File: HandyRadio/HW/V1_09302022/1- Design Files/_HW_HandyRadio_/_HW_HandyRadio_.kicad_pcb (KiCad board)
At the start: 4 copper layers, 74.9 x 74.9 mm, 172 parts, among them J1 MHDR_4POS_1ROW, J2 RECEP_6POS_1ROW, J3 AUDIO_Jack, J4 USB_uAB_RECEP, J5 XH_CONN_2POS_R/A, J6 MHDR_2POS_VERT, K1 DPDT_RELAY, Q1 IRF7401TRPBF, Q2 MMUN2215LT1G, SW1 SPST_NO_RA, SW2 SPST_NO_RA, SW3 SPST_NO_RA, U1 STM32F030F4P6, U2 IR_REC_38KHz, U3 LM4808, U4 MCP73831, U5 AP7361EA, U6 R1211N002B, U7 MIC5365-3.3, U8 EGUARD0502A, U9 SI4735-D60-GU

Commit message: doing placement
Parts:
- C19, C20, C21, C31, C32, C33, C35, C37, C40, D2, EC2, J4, R17, R18, R26, R28, R29, R30, R31, R32: moved to B.Cu
- moved R21 148.1 mm to (201.9, 171.4), turned to 180 degrees
- moved EC5 146.9 mm to (201.9, 168.3), turned to 180 degrees
- moved C20 144.0 mm to (208.9, 163.2), turned to -90 degrees
- moved C19 138.8 mm to (205.1, 163.2), turned to -90 degrees
- moved EC6 137.3 mm to (201.9, 165.1), turned to 180 degrees
- moved R22 136.3 mm to (201.9, 161.9), turned to 180 degrees
- moved R16 135.1 mm to (209.6, 172.7), turned to 180 degrees
- moved EC2 134.7 mm to (208.9, 167.6), turned to -90 degrees
- moved C21 133.8 mm to (205.1, 167.6), turned to 90 degrees
- moved C41 133.2 mm to (160.6, 124.7)
- moved R27 133.2 mm to (154.9, 145.0)
- moved TP16 133.2 mm to (179.1, 125.2)
- moved C39 133.2 mm to (175.1, 121.9)
- moved EC11 133.2 mm to (148.8, 132.1)
- moved EC9 133.2 mm to (140.5, 145.7)
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
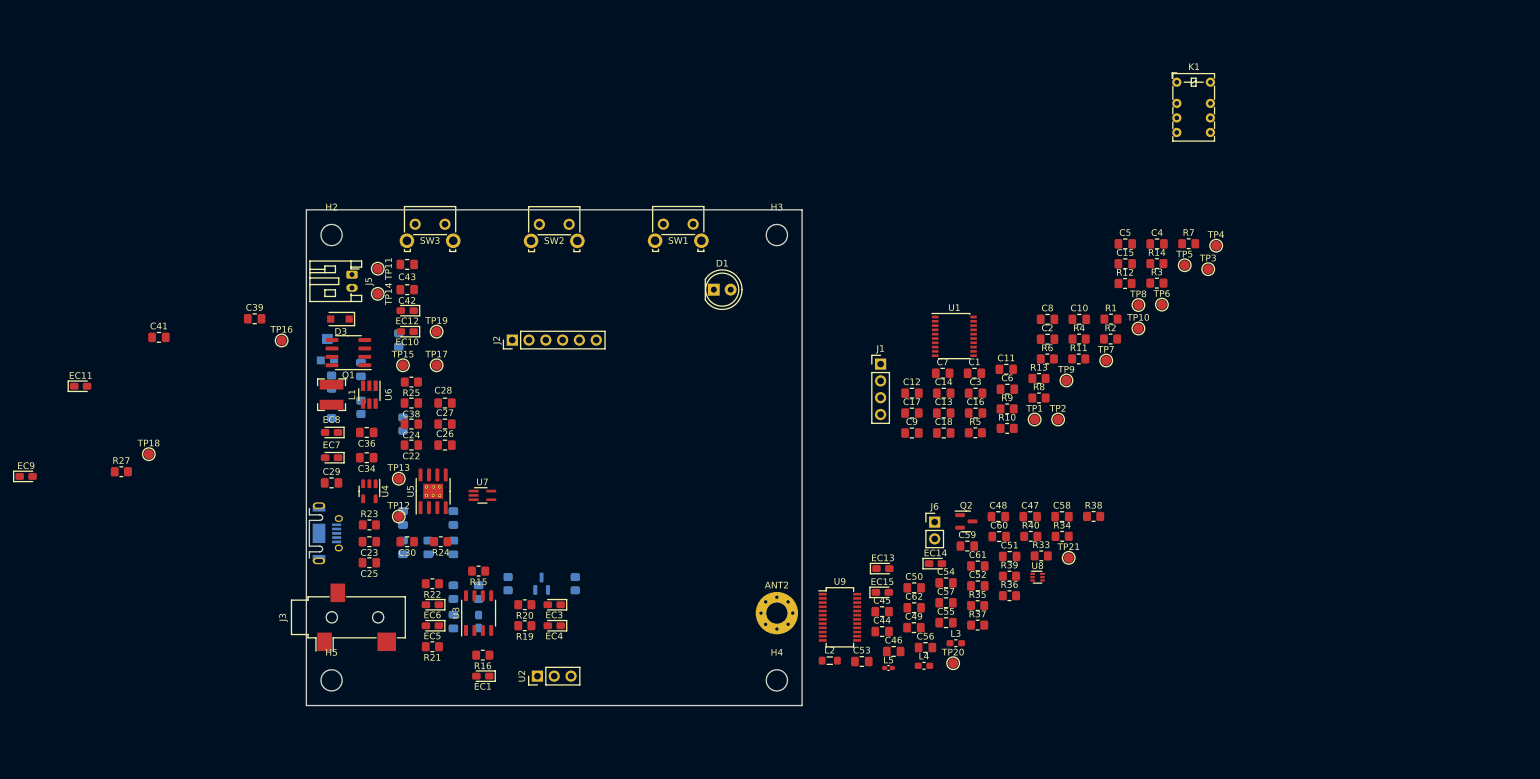
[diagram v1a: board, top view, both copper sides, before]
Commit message: Placement is almost done
Just it needs to checking the footprints, add some 3d and doing routing!
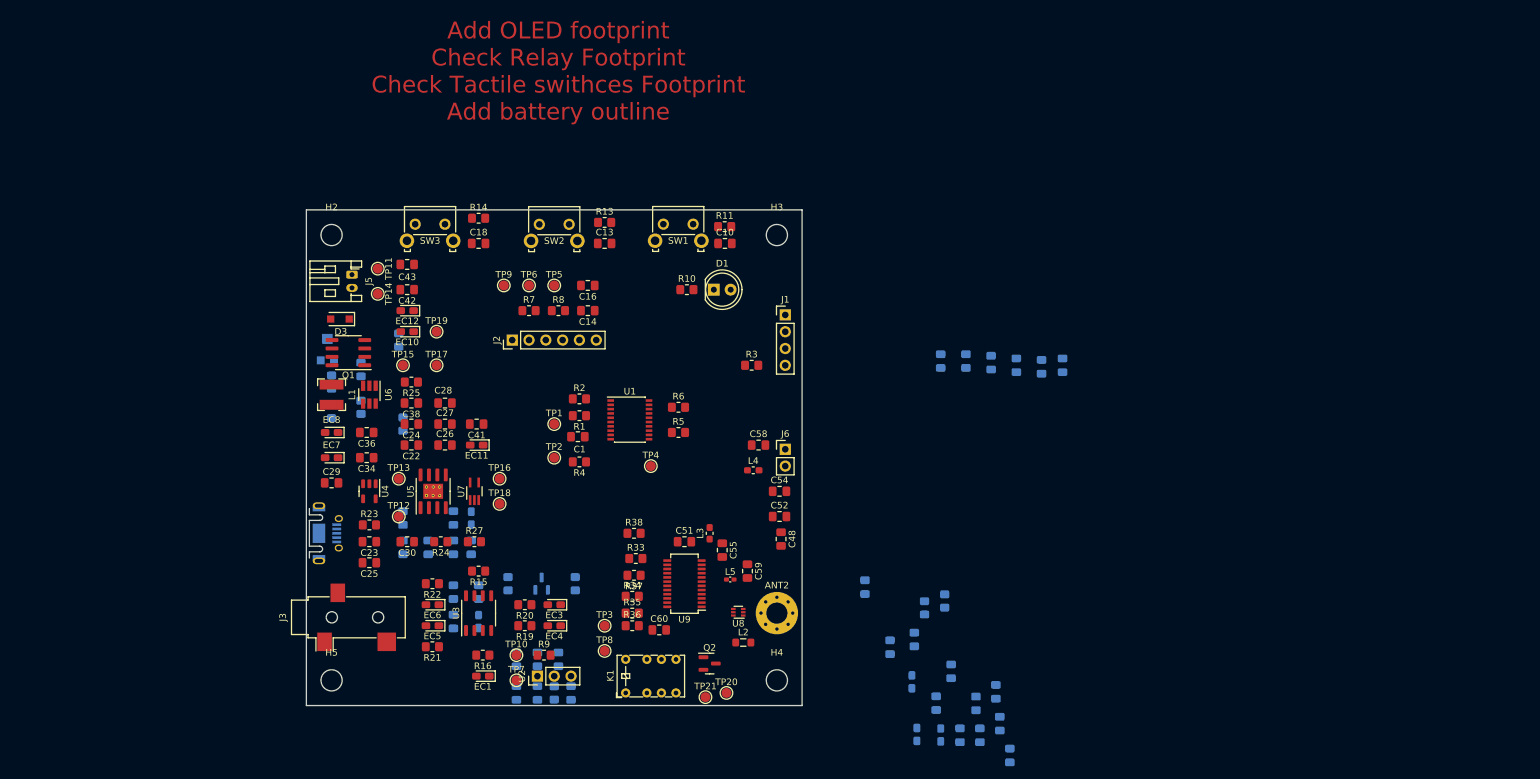
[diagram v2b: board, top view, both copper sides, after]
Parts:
- C11, C12, C15, C17, C2, C3, C39, C4, C44, C45, C46, C47, C49, C5, C50, C53, C56, C57, C6, C61, C62, C7, C8, C9, EC13, EC14, EC15, EC9, R12, R39, R40: moved to B.Cu
- moved K1 124.3 mm to (231.2, 178.4), turned to 90 degrees
- moved C15 109.7 mm to (214.6, 173.4), turned to -90 degrees
- moved TP10 106.2 mm to (214.6, 172.7)
- moved R12 106.2 mm to (220.3, 178.4), turned to -90 degrees
- moved TP3 106.0 mm to (228.0, 168.3)
- moved R14 102.8 mm to (208.9, 106.7)
- moved TP7 101.4 mm to (214.6, 176.5)
- moved R7 100.2 mm to (216.5, 120.7)
- moved C8 98.2 mm to (214.6, 178.4), turned to 90 degrees
- moved TP8 96.1 mm to (228.0, 172.1)
- moved TP6 95.7 mm to (216.5, 116.8)
- moved TP5 95.4 mm to (220.3, 116.8)
- moved TP4 91.7 mm to (234.9, 144.1)
- moved TP9 86.2 mm to (212.7, 116.8)
- moved C11 83.3 mm to (217.8, 173.4), turned to -90 degrees
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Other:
- board text added: "Add OLED footprint Check Relay Footprint Check Tactile swithces Footprint Add battery outline"

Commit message: Working on lib and pcb layout
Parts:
- added DIS1: OLED, _HW_HandyRadio_Footprint:OLED 1.3INCH, F.Cu at (202.7, 126.1)
- J3: footprint Connector_Audio:Jack_3.5mm_CUI_SJ-3523-SMT_Horizontal -> _HW_HandyRadio_Footprint:Jack_3.5mm_CUI_SJ-3524-SMT_Horizontal
- J4: footprint Connector_USB:USB_Micro-AB_Molex_47590-0001 -> _HW_HandyRadio_Footprint:USB_Micro-AB_Molex_47590-0001
- R30: footprint Potentiometer_SMD:Potentiometer_Bourns_TC33X_Vertical -> _HW_HandyRadio_Footprint:Potentiometer_Bourns_TC33X_Vertical
- SW1, SW2, SW3: footprint Button_Switch_THT:SW_Tactile_SKHH_Angled -> _HW_HandyRadio_Footprint:SW_Tact_SKHH_Angled
- U3: footprint Package_SO:SOP-8_3.9x4.9mm_P1.27mm -> _HW_HandyRadio_Footprint:SOP-8_3.9x4.9mm_P1.27mm
- U5: footprint Package_SO:SOIC-8-1EP_3.9x4.9mm_P1.27mm_EP2.29x3mm_ThermalVias -> _HW_HandyRadio_Footprint:Infineon_PG-DSO-8-27_3.9x4.9mm_EP2.65x3mm_ThermalVias
- moved U5 4.13 mm to (199.6, 151.2)
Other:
- board text added: "Add OLED footprint Check Relay Footprint Add battery outline"
- board text removed: "Add OLED footprint Check Relay Footprint Check Tactile swithces Footprint Add battery outline"

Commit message: Some work on PCB, it's paused and will be continued later on
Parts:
- moved TP21 15.4 mm to (227.8, 178.6)
- moved TP20 14.6 mm to (231.8, 178.3)
- moved C51 14.5 mm to (254.3, 158.5)
- moved R33 14.3 mm to (240.3, 146.1)
- moved Q2 14.2 mm to (229.6, 174.2)
- moved R38 14.0 mm to (240.3, 142.7), turned to 180 degrees
- moved R37 13.8 mm to (240.3, 149.4)
- moved R34 13.6 mm to (240.3, 152.9)
- moved R35 13.0 mm to (240.3, 156.2)
- moved U9 12.6 mm to (247.9, 152.1)
- moved TP8 12.1 mm to (236.0, 163.1)
- moved R36 11.8 mm to (240.3, 159.8)
- moved L5 11.3 mm to (254.3, 152.7), turned to 180 degrees
- moved L3 10.6 mm to (254.3, 156.5), turned to 180 degrees
- moved C59 10.3 mm to (254.3, 150.9), turned to 180 degrees
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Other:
- board text added: "Check Relay Footprint"
- board text removed: "Add OLED footprint Check Relay Footprint Add battery outline"

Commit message: serious modification has been done
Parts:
- removed D3: DSS13U, Diode_SMD:D_SOD-123F
- removed EC10, EC12, EC15, EC9: 2u2F/10V, Capacitor_Tantalum_SMD:CP_EIA-2012-12_Kemet-R_Pad1.30x1.05mm_HandSolder
- removed EC11, EC13, EC14, EC7, EC8: 4u7F/6.3V, Capacitor_Tantalum_SMD:CP_EIA-2012-12_Kemet-R_Pad1.30x1.05mm_HandSolder
- removed R40: 330R, Resistor_SMD:R_0805_2012Metric_Pad1.20x1.40mm_HandSolder
- added C63: 6pF, Capacitor_SMD:C_0805_2012Metric_Pad1.18x1.45mm_HandSolder, F.Cu at (255.0, 159.5)
- added C64: 10nF, Capacitor_SMD:C_0805_2012Metric_Pad1.18x1.45mm_HandSolder, B.Cu at (244.3, 156.0)
- added C65: 22nF, Capacitor_SMD:C_0805_2012Metric_Pad1.18x1.45mm_HandSolder, B.Cu at (240.8, 156.0)
- added C66: 3p3F, Capacitor_SMD:C_0805_2012Metric_Pad1.18x1.45mm_HandSolder, F.Cu at (255.0, 149.9)
- added C67: 6pF, Capacitor_SMD:C_0805_2012Metric_Pad1.18x1.45mm_HandSolder, F.Cu at (255.0, 153.4)
- added C68: 22nF, Capacitor_SMD:C_0805_2012Metric_Pad1.18x1.45mm_HandSolder, F.Cu at (241.3, 157.5)
- added C69: 33pF, Capacitor_SMD:C_0805_2012Metric_Pad1.18x1.45mm_HandSolder, B.Cu at (252.0, 155.4)
- added C70: 33pF, Capacitor_SMD:C_0805_2012Metric_Pad1.18x1.45mm_HandSolder, B.Cu at (255.5, 155.4)
- C10, C17, C53: value 100nF -> 10uF
- C11, C49: value 10uF -> 4u7F; moved to F.Cu
- C12, C2, C20, C3, C32, C39, C4, C9, J4: moved to F.Cu
- C13, C16, C25, C26, Q2, R14, R24, R27, R9: moved to B.Cu
- C14: value 4u7F -> 100nF
- C15, C50: value 10uF -> 100nF; moved to F.Cu
- C18, C28, C41: value 100nF -> 1uF; moved to B.Cu
- C19, C22, C30: value 1uF -> 100nF
- C21: value 10nF -> 100nF; moved to F.Cu
- C23: value 4u7F -> 10nF
- C27: value 1uF -> 4u7F; moved to B.Cu
- C29, C34, C42: value 4u7F -> 1uF; moved to B.Cu
- C31: value 1uF -> 4u7F; moved to F.Cu
- C37: value 100nF -> 1uF
- C38: value 220nF -> 4u7F
- C40: value 680pF -> 220nF
- C43: value 4u7F -> 100nF; moved to B.Cu
- C44: value 10uF -> 680pF; moved to F.Cu
- C45: value 10uF -> 1uF
- C46: value 100nF -> 1uF; moved to F.Cu
- C47: value 22nF -> 1uF
- C48: value 33pF -> 1uF
- C5: value 4u7F -> 100nF; moved to F.Cu
- C51: value 18pF -> 4u7F
- C52: value 470nF -> 10uF; moved to B.Cu
- C54: value 3p3F -> 100nF; moved to B.Cu
- C55: value 6pF -> 22nF; moved to B.Cu
- C56: value 10nF -> 33pF; moved to F.Cu
- C57: value 22nF -> 10uF
- C58: value 3p3F -> 10uF; moved to B.Cu
- C59: value 6pF -> 18pF
- C6: value 100nF -> 10uF; moved to F.Cu
- C60: value 22nF -> 470nF
- C61: value 33pF -> 100nF
- C62: value 33pF -> 3p3F; moved to F.Cu
- C7: value 10nF -> 10uF; moved to F.Cu
- C8: value 10uF -> 100nF
- D2: value BAT54ATA -> DSS13U; footprint Package_TO_SOT_SMD:SOT-23 -> Diode_SMD:D_SOD-123F; moved to F.Cu
- EC1: value 1uF/16V -> 4u7F/6.3V
- EC2: value 4u7F/6.3V -> 2u2F/10V; moved to F.Cu
- EC4: value 2u2F/10V -> 4u7F/6.3V; moved to B.Cu
- EC5: value 100uF/6.3V -> 4u7F/6.3V; moved to B.Cu
- EC6: value 100uF/6.3V -> 2u2F/10V; moved to B.Cu
- J3: value AUDIO_Jack -> XH_CONN_2POS_R/A; footprint _HW_HandyRadio_Footprint:Jack_3.5mm_CUI_SJ-3524-SMT_Horizontal -> Connector_JST:JST_PH_S2B-PH-K_1x02_P2.00mm_Horizontal
- K1: footprint Relay_THT:Relay_DPDT_AXICOM_IMSeries_Pitch5.08mm -> Relay_THT:Relay_DPDT_Finder_30.22
- R10: value 1KR -> 10KR; moved to B.Cu
- R11: value 10KR -> 1KR
- R12, R5: value 47R -> 10KR
- R13, R4: value 10KR -> 47R
- R15, R16: value 100KR -> 10KR; moved to B.Cu
- R17, R18: value 1KR -> 3K9R; moved to F.Cu
- R19, R22: value 3K9R -> 10KR
- R20: value 3K9R -> 2KR
- R21: value 3K9R -> 100KR; moved to B.Cu
- R23: value 2KR -> 10KR
- R25: value 100KR -> 30KR
- R26: value 30KR -> 10KR; moved to F.Cu
- R28, R33: value 10KR -> 2KR
- R29: value 2KR -> POT_5KR; footprint Resistor_SMD:R_0805_2012Metric_Pad1.20x1.40mm_HandSolder -> _HW_HandyRadio_Footprint:Potentiometer_Bourns_TC33X_Vertical
- R3: value 1KR -> 10KR
- R30: value POT_5KR -> 82KR; footprint _HW_HandyRadio_Footprint:Potentiometer_Bourns_TC33X_Vertical -> Resistor_SMD:R_0805_2012Metric_Pad1.20x1.40mm_HandSolder; moved to F.Cu
- R31: value 82KR -> 16KR5; moved to F.Cu
- R32: value 16KR5 -> 10KR; moved to F.Cu
- R36: value 2KR -> 100KR
- R37: value 100KR -> 2KR
- R38: value 2KR -> 330R; moved to B.Cu
- U1: value STM32F030F4P6 -> PIC16F15223; footprint Package_SO:SSOP-20_4.4x6.5mm_P0.65mm -> Package_SO:SO-14_3.9x8.65mm_P1.27mm
- U3: value LM4808 -> PAM8302AASCR; footprint _HW_HandyRadio_Footprint:SOP-8_3.9x4.9mm_P1.27mm -> Package_SO:MSOP-8_3x3mm_P0.65mm
- moved C46 104.1 mm to (208.3, 115.8), turned to 180 degrees
- moved C45 97.7 mm to (205.2, 124.0), turned to 90 degrees
- moved C49 97.1 mm to (195.1, 141.2), turned to 0 degrees
- moved C44 92.6 mm to (197.6, 153.4), turned to 0 degrees
- moved C50 90.1 mm to (208.3, 122.9), turned to 180 degrees
- moved C5 87.4 mm to (208.3, 146.3), turned to 180 degrees
- moved C4 82.2 mm to (215.4, 137.2), turned to 0 degrees
- moved C6 74.8 mm to (221.5, 165.6), turned to 0 degrees
- moved C2 70.2 mm to (220.5, 137.2), turned to 180 degrees
- moved C47 70.1 mm to (208.8, 124.0), turned to 90 degrees
- moved C8 65.5 mm to (228.1, 114.3)
- moved R13 65.2 mm to (226.1, 172.5), turned to 180 degrees
- moved R16 64.9 mm to (194.1, 109.7), turned to 90 degrees
- moved C7 64.6 mm to (226.1, 165.6), turned to 180 degrees
- moved R12 64.6 mm to (212.9, 114.3), turned to 90 degrees
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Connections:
- net /BLOCK DIAGRAM/MCU, RTC, OLED, PB, LED/MCU_NRST renamed /BLOCK DIAGRAM/MCU, RTC, OLED, PB, LED/~{MCLR}
- C10 pad 2: /BLOCK DIAGRAM/MCU, RTC, OLED, PB, LED/PB_3 -> +3V3
- C13 pad 2: /BLOCK DIAGRAM/MCU, RTC, OLED, PB, LED/PB_2 -> Net-(C13-Pad2)
- C15 pad 2: +3V3 -> Net-(C15-Pad2)
- C16 pad 2: +3V3 -> Net-(C16-Pad2)
- C17 pad 1: GND -> +5V
- C17 pad 2: Net-(C17-Pad2) -> GND
- C18 pad 2: /BLOCK DIAGRAM/MCU, RTC, OLED, PB, LED/PB_1 -> +5V
- C20 pad 1: GND -> /BLOCK DIAGRAM/MCU, RTC, OLED, PB, LED/BEEP_OUPUT
- C20 pad 2: +5V -> Net-(C20-Pad2)
- C21 pad 1: GND -> Net-(C21-Pad1)
- C21 pad 2: +5V -> Net-(C20-Pad2)
- C22 pad 1: +6V -> GND
- C22 pad 2: GND -> Net-(C22-Pad2)
- C23 pad 2: VBUS -> +5V
- C27 pad 1: +6V -> GND
- C27 pad 2: GND -> VBUS
- C28 pad 1: GND -> +6V
- C28 pad 2: +6V -> GND
- C29 pad 1: GND -> +6V
- C29 pad 2: +BATT -> GND
- C30 pad 1: +5V -> GND
- C30 pad 2: GND -> +6V
- C31 pad 1: +5V -> GND
- C31 pad 2: GND -> +BATT
- C34 pad 1: GND -> +5V
- C34 pad 2: +BATT -> GND
- C37 pad 1: GND -> +5V
- C37 pad 2: +5V -> GND
- C38 pad 2: /BLOCK DIAGRAM/DCDC PWS/DELAY -> +BATT
- C40 pad 1: Net-(C40-Pad1) -> GND
- C40 pad 2: +6V -> /BLOCK DIAGRAM/DCDC PWS/DELAY
- C41 pad 2: +3.3V -> +5V
- C42 pad 1: +6V -> GND
- C42 pad 2: GND -> +5V
- C43 pad 2: +6V -> +5V
- C44 pad 1: GND -> Net-(C44-Pad1)
- C44 pad 2: +3V3 -> +6V
- C45 pad 2: +3V3 -> +3.3V
- C46 pad 2: +3V3 -> +3.3V
- C47 pad 2: +3V3 -> +3.3V
- C48 pad 1: Net-(C48-Pad1) -> GND
- C48 pad 2: Net-(C48-Pad2) -> +3.3V
- C49 pad 1: GND -> +6V
- C49 pad 2: +5V -> GND
- C5 pad 1: GND -> /BLOCK DIAGRAM/MCU, RTC, OLED, PB, LED/LED_IND
- C5 pad 2: +3V3 -> /BLOCK DIAGRAM/MCU, RTC, OLED, PB, LED/BEEP_OUPUT
- C50 pad 2: +5V -> +3.3V
- C51 pad 1: Net-(C51-Pad1) -> GND
- C51 pad 2: Net-(C51-Pad2) -> +6V
- C52 pad 1: Net-(C52-Pad1) -> GND
- C52 pad 2: Net-(C52-Pad2) -> +3V3
- C53 pad 2: +5V -> +3V3
- C54 pad 2: Net-(C52-Pad2) -> +3V3
- C55 pad 2: Net-(C51-Pad2) -> +3V3
- C56 pad 1: GND -> Net-(K1-Pad22)
- C56 pad 2: +5V -> Net-(K1-Pad21)
- C58 pad 2: /BLOCK DIAGRAM/RF RECEIVER/AMI -> +5V
- C59 pad 1: GND -> Net-(C59-Pad1)
- C59 pad 2: /BLOCK DIAGRAM/RF RECEIVER/FMI -> Net-(C59-Pad2)
- C60 pad 1: GND -> Net-(C60-Pad1)
- C61 pad 2: /BLOCK DIAGRAM/RF RECEIVER/GPO2 -> +5V
- C62 pad 2: /BLOCK DIAGRAM/RF RECEIVER/GPO1 -> Net-(C60-Pad2)
- C8 pad 2: +3V3 -> Net-(C8-Pad2)
- D2 pad 1: Net-(D2-Pad1) -> +6V
- EC1 pad 1: /BLOCK DIAGRAM/AUDIO AMP/IN+ -> +BATT
- EC2 pad 1: +5V -> +6V
- EC3 pad 1: Net-(EC3-Pad1) -> +6V
- EC3 pad 2: /BLOCK DIAGRAM/AUDIO AMP/AUDIO_L -> GND
- EC4 pad 1: Net-(EC4-Pad1) -> +3V3
- EC4 pad 2: /BLOCK DIAGRAM/AUDIO AMP/AUDIO_R -> GND
- EC5 pad 1: Net-(EC5-Pad1) -> +5V
- EC5 pad 2: /BLOCK DIAGRAM/AUDIO AMP/AUDIO_LEFT -> GND
- EC6 pad 1: Net-(EC6-Pad1) -> +5V
- EC6 pad 2: /BLOCK DIAGRAM/AUDIO AMP/AUDIO_RIGHT -> GND
- J1 pad 2: /BLOCK DIAGRAM/MCU, RTC, OLED, PB, LED/SWCLK -> /BLOCK DIAGRAM/MCU, RTC, OLED, PB, LED/ICSPCLK
- J1 pad 3: /BLOCK DIAGRAM/MCU, RTC, OLED, PB, LED/SWDIO -> /BLOCK DIAGRAM/MCU, RTC, OLED, PB, LED/ICSPDAT
- J4 pad 1: VBUS -> GND
- J4 pad 5: GND -> VBUS
- J6 pad 2: Net-(C48-Pad1) -> Net-(K1-Pad22)
- L1 pad 2: Net-(D3-Pad2) -> Net-(D2-Pad2)
- L2 pad 1: Net-(K1-Pad8) -> Net-(K1-Pad24)
- L3 pad 1: Net-(C51-Pad2) -> Net-(C59-Pad2)
- L4 pad 1: Net-(C52-Pad2) -> Net-(C60-Pad2)
- L5 pad 1: Net-(C51-Pad2) -> Net-(C59-Pad2)
- Q1 pad 5: Net-(D3-Pad2) -> Net-(D2-Pad2)
- Q1 pad 6: Net-(D3-Pad2) -> Net-(D2-Pad2)
- Q1 pad 7: Net-(D3-Pad2) -> Net-(D2-Pad2)
- Q1 pad 8: Net-(D3-Pad2) -> Net-(D2-Pad2)
- Q2 pad 3: Net-(K1-Pad5) -> Net-(K1-PadA2)
- R10 pad 1: /BLOCK DIAGRAM/MCU, RTC, OLED, PB, LED/LED_IND -> Net-(C8-Pad2)
- R10 pad 2: Net-(D1-Pad1) -> +3V3
- R11 pad 1: GND -> /BLOCK DIAGRAM/MCU, RTC, OLED, PB, LED/LED_IND
- R11 pad 2: /BLOCK DIAGRAM/MCU, RTC, OLED, PB, LED/PB_3 -> Net-(D1-Pad1)
- R12 pad 1: +3V3 -> /BLOCK DIAGRAM/MCU, RTC, OLED, PB, LED/ICSPCLK
- R12 pad 2: Net-(C17-Pad2) -> Net-(C13-Pad2)
- R13 pad 1: GND -> +3V3
- R13 pad 2: /BLOCK DIAGRAM/MCU, RTC, OLED, PB, LED/PB_2 -> Net-(C15-Pad2)
- R14 pad 1: GND -> Net-(C13-Pad2)
- R14 pad 2: /BLOCK DIAGRAM/MCU, RTC, OLED, PB, LED/PB_1 -> +3V3
- R15 pad 1: /BLOCK DIAGRAM/AUDIO AMP/IN+ -> Net-(C16-Pad2)
- R15 pad 2: +5V -> /BLOCK DIAGRAM/MCU, RTC, OLED, PB, LED/ICSPDAT
- R16 pad 1: GND -> Net-(C16-Pad2)
- R16 pad 2: /BLOCK DIAGRAM/AUDIO AMP/IN+ -> +3V3
- R17 pad 1: Net-(D2-Pad2) -> /BLOCK DIAGRAM/AUDIO AMP/AUDIO_L
- R17 pad 2: /BLOCK DIAGRAM/AUDIO AMP/AUDIO_L -> Net-(C21-Pad1)
- R18 pad 1: Net-(D2-Pad1) -> /BLOCK DIAGRAM/AUDIO AMP/AUDIO_R
- R18 pad 2: /BLOCK DIAGRAM/AUDIO AMP/AUDIO_R -> Net-(C21-Pad1)
- R19 pad 1: Net-(EC3-Pad1) -> +5V
- R19 pad 2: /BLOCK DIAGRAM/AUDIO AMP/INA- -> Net-(R19-Pad2)
- R2 pad 1: GND -> Net-(J1-Pad4)
- R2 pad 2: /BLOCK DIAGRAM/MCU, RTC, OLED, PB, LED/MCU_BOOT0 -> +3V3
- R20 pad 1: Net-(EC4-Pad1) -> GND
- R20 pad 2: /BLOCK DIAGRAM/AUDIO AMP/INB- -> /BLOCK DIAGRAM/DCDC PWS/PROG
- R21 pad 1: /BLOCK DIAGRAM/AUDIO AMP/INA- -> +6V
- R21 pad 2: Net-(EC5-Pad1) -> Net-(R21-Pad2)
- R22 pad 1: /BLOCK DIAGRAM/AUDIO AMP/INB- -> /BLOCK DIAGRAM/MCU, RTC, OLED, PB, LED/BATT_STAT
- R22 pad 2: Net-(EC6-Pad1) -> +BATT
- R23 pad 1: VBUS -> GND
- R23 pad 2: Net-(R23-Pad2) -> /BLOCK DIAGRAM/MCU, RTC, OLED, PB, LED/BATT_STAT
- R24 pad 1: +6V -> +BATT
- R25 pad 1: +BATT -> Net-(R25-Pad1)
- R25 pad 2: Net-(R25-Pad2) -> Net-(C44-Pad1)
- R26 pad 1: Net-(R26-Pad1) -> +5V
- R26 pad 2: Net-(C40-Pad1) -> /BLOCK DIAGRAM/DCDC PWS/LDO3V3_EN
- R27 pad 1: +5V -> Net-(R27-Pad1)
- R27 pad 2: Net-(R27-Pad2) -> Net-(C44-Pad1)
- R28 pad 2: Net-(C40-Pad1) -> Net-(R27-Pad1)
- R29 pad 1: Net-(R29-Pad1) -> Net-(R28-Pad1)
- R3 pad 1: Net-(J1-Pad4) -> Net-(R3-Pad1)
- R3 pad 2: +3V3 -> /BLOCK DIAGRAM/MCU, RTC, OLED, PB, LED/OLED_RST
- R30 pad 1: Net-(R29-Pad1) -> Net-(C44-Pad1)
- R30 pad 2: Net-(R29-Pad1) -> +6V
- R31 pad 1: Net-(C40-Pad1) -> GND
- R31 pad 2: +6V -> Net-(C44-Pad1)
- R32 pad 2: Net-(C40-Pad1) -> /BLOCK DIAGRAM/RF RECEIVER/~{RST}
- R33 pad 1: GND -> /BLOCK DIAGRAM/MCU, RTC, OLED, PB, LED/I2C_SCL
- R33 pad 2: /BLOCK DIAGRAM/RF RECEIVER/~{RST} -> /BLOCK DIAGRAM/RF RECEIVER/SCLK
- R34 pad 1: /BLOCK DIAGRAM/MCU, RTC, OLED, PB, LED/I2C_SCL -> /BLOCK DIAGRAM/MCU, RTC, OLED, PB, LED/I2C_SDA
- R34 pad 2: /BLOCK DIAGRAM/RF RECEIVER/SCLK -> /BLOCK DIAGRAM/RF RECEIVER/SDIO
- R35 pad 1: /BLOCK DIAGRAM/MCU, RTC, OLED, PB, LED/I2C_SDA -> /BLOCK DIAGRAM/MCU, RTC, OLED, PB, LED/SI47_CLK
- R35 pad 2: /BLOCK DIAGRAM/RF RECEIVER/SDIO -> /BLOCK DIAGRAM/RF RECEIVER/RCLK
- R36 pad 1: /BLOCK DIAGRAM/MCU, RTC, OLED, PB, LED/SI47_CLK -> /BLOCK DIAGRAM/RF RECEIVER/~{SEN}
- R36 pad 2: /BLOCK DIAGRAM/RF RECEIVER/RCLK -> GND
- R37 pad 1: /BLOCK DIAGRAM/RF RECEIVER/~{SEN} -> /BLOCK DIAGRAM/RF RECEIVER/~{RST}
- R37 pad 2: GND -> +3V3
- R38 pad 1: /BLOCK DIAGRAM/RF RECEIVER/~{RST} -> /BLOCK DIAGRAM/RF RECEIVER/GPO1
- R39 pad 1: /BLOCK DIAGRAM/RF RECEIVER/GPO1 -> /BLOCK DIAGRAM/RF RECEIVER/GPO2
- R39 pad 2: +3V3 -> GND
- R4 pad 1: /BLOCK DIAGRAM/MCU, RTC, OLED, PB, LED/BEEP_OUPUT -> /BLOCK DIAGRAM/MCU, RTC, OLED, PB, LED/SI47_CLK
- R4 pad 2: /BLOCK DIAGRAM/AUDIO AMP/BEEP_SIG -> /BLOCK DIAGRAM/MCU, RTC, OLED, PB, LED/SI47_CLK
- R5 pad 1: /BLOCK DIAGRAM/MCU, RTC, OLED, PB, LED/SI47_CLK -> /BLOCK DIAGRAM/MCU, RTC, OLED, PB, LED/BEEP_OUPUT
- R5 pad 2: /BLOCK DIAGRAM/MCU, RTC, OLED, PB, LED/SI47_CLK -> GND
- R6 pad 1: /BLOCK DIAGRAM/MCU, RTC, OLED, PB, LED/SWDIO -> /BLOCK DIAGRAM/MCU, RTC, OLED, PB, LED/I2C_SDA
- R6 pad 2: /BLOCK DIAGRAM/MCU, RTC, OLED, PB, LED/OLED_RST -> +3V3
- R7 pad 1: /BLOCK DIAGRAM/MCU, RTC, OLED, PB, LED/I2C_SDA -> /BLOCK DIAGRAM/MCU, RTC, OLED, PB, LED/I2C_SCL
- R8 pad 1: /BLOCK DIAGRAM/MCU, RTC, OLED, PB, LED/I2C_SCL -> /BLOCK DIAGRAM/MCU, RTC, OLED, PB, LED/IR_INPUT
- R9 pad 1: /BLOCK DIAGRAM/MCU, RTC, OLED, PB, LED/IR_INPUT -> Net-(C8-Pad2)
- R9 pad 2: +3V3 -> /BLOCK DIAGRAM/MCU, RTC, OLED, PB, LED/PB_1
- SW1 pad 1: +3V3 -> Net-(C8-Pad2)
- SW1 pad 2: /BLOCK DIAGRAM/MCU, RTC, OLED, PB, LED/PB_3 -> GND
- SW2 pad 1: +3V3 -> Net-(C13-Pad2)
- SW2 pad 2: /BLOCK DIAGRAM/MCU, RTC, OLED, PB, LED/PB_2 -> GND
- SW3 pad 1: +3V3 -> Net-(C16-Pad2)
- SW3 pad 2: /BLOCK DIAGRAM/MCU, RTC, OLED, PB, LED/PB_1 -> GND
- TP15 pad 1: Net-(C40-Pad1) -> Net-(C44-Pad1)
- TP16 pad 1: +3.3V -> GND
- TP17 pad 1: GND -> +3.3V
- TP3 pad 1: /BLOCK DIAGRAM/MCU, RTC, OLED, PB, LED/SI47_CLK -> /BLOCK DIAGRAM/MCU, RTC, OLED, PB, LED/I2C_SCL
- TP4 pad 1: /BLOCK DIAGRAM/MCU, RTC, OLED, PB, LED/BATT_STAT -> /BLOCK DIAGRAM/MCU, RTC, OLED, PB, LED/I2C_SDA
- TP5 pad 1: /BLOCK DIAGRAM/MCU, RTC, OLED, PB, LED/I2C_SCL -> /BLOCK DIAGRAM/MCU, RTC, OLED, PB, LED/SI47_CLK
- TP6 pad 1: /BLOCK DIAGRAM/MCU, RTC, OLED, PB, LED/I2C_SDA -> GND
- TP9 pad 1: GND -> /BLOCK DIAGRAM/MCU, RTC, OLED, PB, LED/BATT_STAT
- U1 pad 1: /BLOCK DIAGRAM/MCU, RTC, OLED, PB, LED/MCU_BOOT0 -> +3V3
- U1 pad 10: /BLOCK DIAGRAM/MCU, RTC, OLED, PB, LED/BEEP_OUPUT -> /BLOCK DIAGRAM/MCU, RTC, OLED, PB, LED/I2C_SCL
- U1 pad 11: /BLOCK DIAGRAM/MCU, RTC, OLED, PB, LED/BATT_STAT -> /BLOCK DIAGRAM/MCU, RTC, OLED, PB, LED/PB_1
- U1 pad 12: /BLOCK DIAGRAM/MCU, RTC, OLED, PB, LED/IR_INPUT -> /BLOCK DIAGRAM/MCU, RTC, OLED, PB, LED/ICSPCLK
- U1 pad 13: /BLOCK DIAGRAM/MCU, RTC, OLED, PB, LED/SI47_CLK -> /BLOCK DIAGRAM/MCU, RTC, OLED, PB, LED/ICSPDAT
- U1 pad 14: /BLOCK DIAGRAM/MCU, RTC, OLED, PB, LED/LED_IND -> GND
- U1 pad 2: unconnected-(U1-Pad2) -> /BLOCK DIAGRAM/MCU, RTC, OLED, PB, LED/IR_INPUT
- U1 pad 3: unconnected-(U1-Pad3) -> /BLOCK DIAGRAM/MCU, RTC, OLED, PB, LED/BATT_STAT
- U1 pad 5: +3V3 -> /BLOCK DIAGRAM/MCU, RTC, OLED, PB, LED/LED_IND
- U1 pad 6: /BLOCK DIAGRAM/MCU, RTC, OLED, PB, LED/PB_1 -> /BLOCK DIAGRAM/MCU, RTC, OLED, PB, LED/~{FM}/SW_SEL
- U1 pad 7: /BLOCK DIAGRAM/MCU, RTC, OLED, PB, LED/PB_2 -> /BLOCK DIAGRAM/MCU, RTC, OLED, PB, LED/SI47_CLK
- U1 pad 8: /BLOCK DIAGRAM/MCU, RTC, OLED, PB, LED/PB_3 -> Net-(R3-Pad1)
- U1 pad 9: /BLOCK DIAGRAM/MCU, RTC, OLED, PB, LED/~{FM}/SW_SEL -> /BLOCK DIAGRAM/MCU, RTC, OLED, PB, LED/I2C_SDA
- U2 pad 3: Net-(C17-Pad2) -> Net-(C15-Pad2)
- U3 pad 1: Net-(EC5-Pad1) -> Net-(R19-Pad2)
- U3 pad 2: /BLOCK DIAGRAM/AUDIO AMP/INA- -> unconnected-(U3-Pad2)
- U3 pad 3: /BLOCK DIAGRAM/AUDIO AMP/IN+ -> Net-(C20-Pad2)
- U3 pad 4: GND -> Net-(C22-Pad2)
- U3 pad 5: /BLOCK DIAGRAM/AUDIO AMP/IN+ -> /BLOCK DIAGRAM/AUDIO AMP/SPK+
- U3 pad 6: /BLOCK DIAGRAM/AUDIO AMP/INB- -> +5V
- U3 pad 7: Net-(EC6-Pad1) -> GND
- U3 pad 8: +5V -> /BLOCK DIAGRAM/AUDIO AMP/SPK-
- U4 pad 5: Net-(R23-Pad2) -> /BLOCK DIAGRAM/DCDC PWS/PROG
- U5 pad 2: Net-(R24-Pad2) -> Net-(R21-Pad2)
- U6 pad 2: Net-(R25-Pad2) -> Net-(R24-Pad2)
- U6 pad 3: Net-(R26-Pad1) -> Net-(R25-Pad1)
- U7 pad 3: Net-(R27-Pad2) -> /BLOCK DIAGRAM/DCDC PWS/LDO3V3_EN
- U8 pad 3: Net-(C48-Pad2) -> Net-(K1-Pad21)
- U8 pad 4: Net-(C52-Pad1) -> Net-(C60-Pad1)
- U8 pad 6: Net-(C51-Pad1) -> Net-(C59-Pad1)
- U9 pad 22: Net-(C60-Pad2) -> Net-(C68-Pad2)
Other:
- board text removed: "Check Relay Footprint"

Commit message: layout is in progress
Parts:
- moved C25 3.32 mm to (193.5, 169.4)
- moved C27 3.32 mm to (189.9, 169.4)
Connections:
- net Net-(D2-Pad2) renamed /BLOCK DIAGRAM/DCDC PWS/L_O
- C45 pad 2: +3.3V -> +3V3
- C46 pad 2: +3.3V -> +3V3
- C47 pad 2: +3.3V -> +3V3
- C48 pad 2: +3.3V -> +3V3
- C50 pad 2: +3.3V -> +3V3
- TP17 pad 1: +3.3V -> +3V3
- U7 pad 5: +3.3V -> +3V3
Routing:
- net GND: track 0.00 -> 47.8 mm, vias 0 -> 27
- net +6V: track 0.00 -> 26.0 mm, vias 0 -> 14
- net +BATT: track 0.00 -> 25.5 mm, vias 0 -> 12
- net Net-(C44-Pad1): track 0.00 -> 14.1 mm, vias 0 -> 1
- net /BLOCK DIAGRAM/DCDC PWS/DELAY: track 0.00 -> 11.2 mm, vias 0 -> 1
- net /BLOCK DIAGRAM/MCU, RTC, OLED, PB, LED/BATT_STAT: track 0.00 -> 10.4 mm
- net Net-(R24-Pad2): track 0.00 -> 7.84 mm, vias 0 -> 1
- net Net-(R28-Pad1): track 0.00 -> 7.35 mm
- net VBUS: track 0.00 -> 5.93 mm, vias 0 -> 2
- net Net-(Q1-Pad4): track 0.00 -> 5.67 mm
- net /BLOCK DIAGRAM/DCDC PWS/PROG: track 0.00 -> 5.31 mm
- net Net-(R27-Pad1): track 0.00 -> 4.83 mm
- net Net-(R25-Pad1): track 0.00 -> 3.98 mm
- net +5V: track 0.00 -> 1.78 mm, vias 0 -> 1
- added copper zone on In2.Cu, net +3V3
- added copper zone on In2.Cu, net +5V
- added copper zone on In2.Cu, net +6V
- added copper zone on F.Cu, net +BATT
- added copper zone on In2.Cu, net +BATT
- added copper zone on F.Cu, net /BLOCK DIAGRAM/DCDC PWS/L_O
- added copper zone on F.Cu, net GND
- added copper zone on In1.Cu, net GND
- added copper zone on F.Cu, net VBUS

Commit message: layout has been done, only checking rules has been left
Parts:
- C55, C65: moved to F.Cu
- moved EC6 18.9 mm to (229.0, 163.1)
- moved EC5 18.5 mm to (225.9, 163.1)
- moved EC4 15.2 mm to (229.1, 152.3)
- moved C61 14.2 mm to (235.6, 163.0), turned to 90 degrees
- moved C64 14.0 mm to (232.2, 163.0), turned to 90 degrees
- moved C52 13.3 mm to (232.3, 152.4), turned to 90 degrees
- moved R2 11.9 mm to (251.2, 121.6)
- moved C33 11.0 mm to (200.9, 126.6), turned to 90 degrees
- moved C54 10.8 mm to (238.7, 152.5), turned to 90 degrees
- moved C37 10.8 mm to (197.6, 126.6), turned to 90 degrees
- moved C29 8.49 mm to (185.9, 132.6), turned to -90 degrees
- moved C53 7.72 mm to (235.5, 152.4), turned to 90 degrees
- moved J1 7.57 mm to (255.4, 129.2), turned to 180 degrees
- moved C55 7.35 mm to (241.3, 155.1), turned to 0 degrees
- moved C65 4.79 mm to (241.3, 160.7), turned to 0 degrees
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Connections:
- D1 pad 2: +3.3V -> +3V3
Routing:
- net GND: track 47.8 -> 198.6 mm, vias 27 -> 98
- net +3V3: track 0.00 -> 97.4 mm, vias 0 -> 31
- net /BLOCK DIAGRAM/MCU, RTC, OLED, PB, LED/ICSPDAT: track 0.00 -> 90.5 mm, vias 0 -> 1
- net /BLOCK DIAGRAM/MCU, RTC, OLED, PB, LED/ICSPCLK: track 0.00 -> 76.8 mm, vias 0 -> 1
- net /BLOCK DIAGRAM/MCU, RTC, OLED, PB, LED/BATT_STAT: track 10.4 -> 79.5 mm, vias 0 -> 2
- net +5V: track 1.78 -> 65.5 mm, vias 1 -> 26
- net /BLOCK DIAGRAM/MCU, RTC, OLED, PB, LED/LED_IND: track 0.00 -> 61.1 mm, vias 0 -> 2
- net /BLOCK DIAGRAM/MCU, RTC, OLED, PB, LED/IR_INPUT: track 0.00 -> 49.7 mm, vias 0 -> 1
- net /BLOCK DIAGRAM/MCU, RTC, OLED, PB, LED/I2C_SDA: track 0.00 -> 49.2 mm, vias 0 -> 1
- net /BLOCK DIAGRAM/MCU, RTC, OLED, PB, LED/~{FM}/SW_SEL: track 0.00 -> 47.0 mm, vias 0 -> 2
- net /BLOCK DIAGRAM/MCU, RTC, OLED, PB, LED/I2C_SCL: track 0.00 -> 46.6 mm, vias 0 -> 1
- net Net-(C56-Pad1): track 0.00 -> 39.7 mm
- net /BLOCK DIAGRAM/MCU, RTC, OLED, PB, LED/PB_1: track 0.00 -> 37.2 mm, vias 0 -> 1
- net Net-(R3-Pad1): track 0.00 -> 35.9 mm, vias 0 -> 2
- net /BLOCK DIAGRAM/MCU, RTC, OLED, PB, LED/BEEP_OUPUT: track 0.00 -> 31.2 mm
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- added copper zone on F.Cu, net +3V3
- added copper zone on F.Cu, net +5V
- added copper zone on F.Cu, net +6V

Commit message: almost critical errors have been corrected
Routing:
- net Net-(R21-Pad2): track 27.1 -> 18.5 mm, vias 2 -> 1
- net +3V3: track 97.4 -> 95.8 mm, vias 31 -> 30
- net /BLOCK DIAGRAM/RF RECEIVER/GPO2: track 6.84 -> 8.05 mm
- net Net-(C22-Pad2): track 14.4 -> 13.4 mm
- net +BATT: track 25.5 -> 24.5 mm
